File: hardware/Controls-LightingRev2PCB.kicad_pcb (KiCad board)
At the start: 2 copper layers, 50 x 53.5 mm, 53 parts, among them IC1 LM74502HDDFR, IC3 TLV70130DBVR, J1 MX150_02x08_RightAngle, J3 53307-2471, Q2 IRLML0030, Q3 IRLML0030, Q4 PSMN8R5-40MSDX, U1 TLV2371DBV, U2 INA241A5xD, U3 INA241A5xD, U4 INA241A5xD, U5 SN74LV1T34DBV, U8 TLV2371DBV, U9 TLV2371DBV

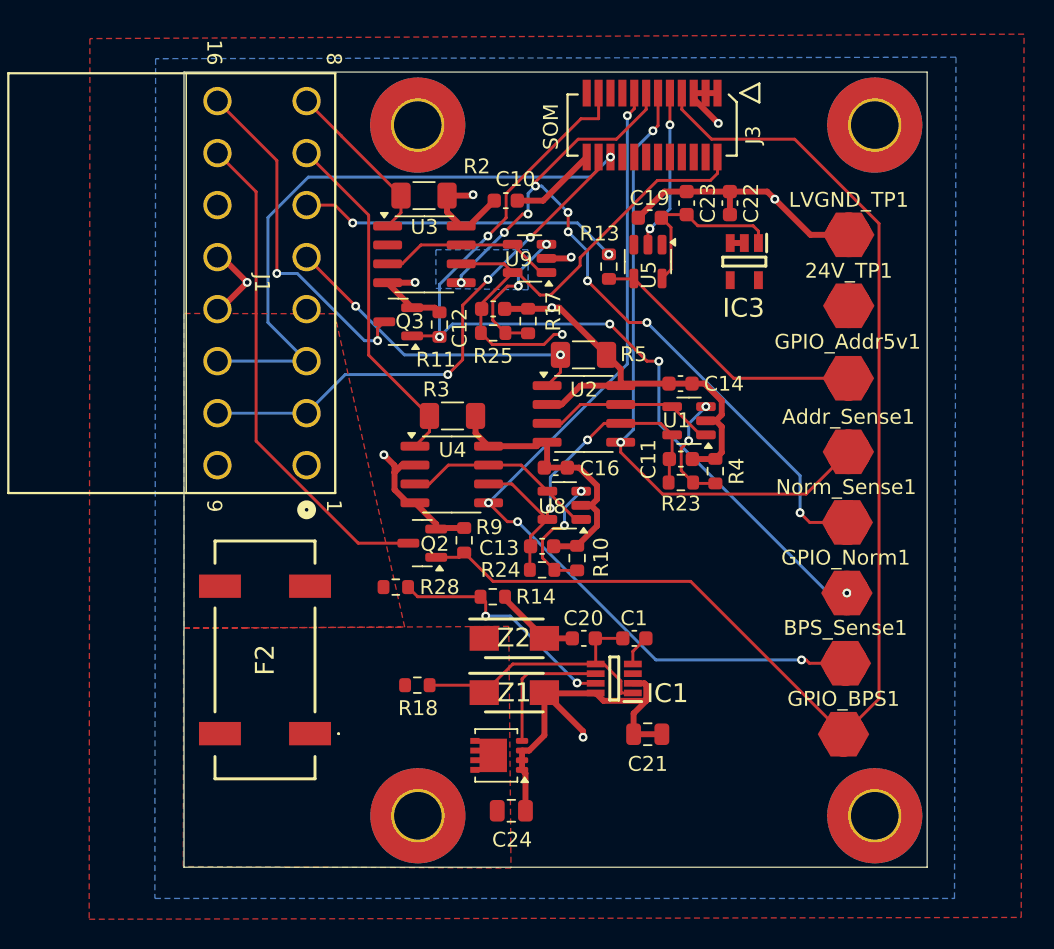
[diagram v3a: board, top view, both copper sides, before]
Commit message: Test points added
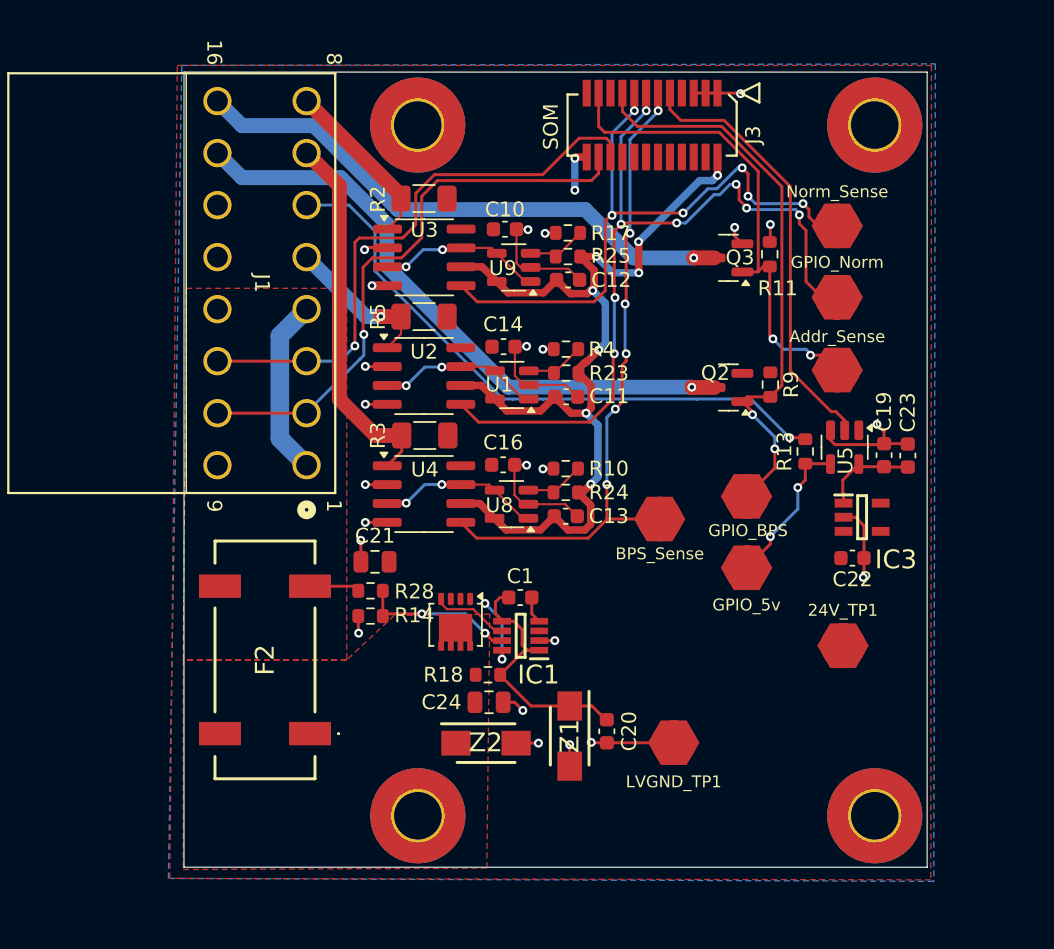
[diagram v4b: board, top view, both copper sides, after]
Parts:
- removed Addr_Sense1, BPS_Sense1, GPIO_Addr5v1, GPIO_BPS1, GPIO_Norm1, Norm_Sense1: TestPoint, UTSVT_Special:TestPoint_HEX_3mmID
- added Addr_Sense: TestPoint, UTSVT_Special:TestPoint_HEX_3mmID, F.Cu at (124.8, 37.0)
- added BPS_Sense: TestPoint, UTSVT_Special:TestPoint_HEX_3mmID, F.Cu at (112.8, 51.9)
- added GPIO_5v: TestPoint, UTSVT_Special:TestPoint_HEX_3mmID, F.Cu at (118.7, 55.2)
- added GPIO_BPS: TestPoint, UTSVT_Special:TestPoint_HEX_3mmID, F.Cu at (118.7, 50.4)
- added GPIO_Norm: TestPoint, UTSVT_Special:TestPoint_HEX_3mmID, F.Cu at (124.8, 41.9)
- added Norm_Sense: TestPoint, UTSVT_Special:TestPoint_HEX_3mmID, F.Cu at (124.8, 32.2)
- moved LVGND_TP1 36.1 mm to (113.8, 67.0)
- moved C22 25.3 mm to (125.8, 54.5), turned to 180 degrees
- moved Q2 23.1 mm to (117.5, 43.1)
- moved R9 23.1 mm to (120.3, 42.9)
- moved 24V_TP1 22.9 mm to (125.2, 60.4)
- moved R11 22.7 mm to (120.3, 34.1)
- moved Q3 22.6 mm to (117.5, 34.4)
- moved C23 22.6 mm to (129.6, 47.6)
- moved C19 22.4 mm to (128.0, 47.6), turned to -90 degrees
- moved C21 21.7 mm to (93.7, 54.8)
- moved IC3 18.9 mm to (126.5, 51.8), turned to 0 degrees
- moved U5 18.2 mm to (125.3, 47.1)
- moved R13 18.1 mm to (122.7, 47.4)
- moved R4 13.0 mm to (106.5, 40.5), turned to 180 degrees
- moved C14 12.2 mm to (102.3, 40.3)
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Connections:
- C10 pad 1: +24V -> Addressable_GND
- C11 pad 1: +24V -> Addressable_GND
- C12 pad 1: +24V -> Addressable_GND
- C13 pad 1: +24V -> Addressable_GND
- C14 pad 1: +24V -> Addressable_GND
- C16 pad 1: +24V -> Addressable_GND
- C19 pad 1: +24V -> Addressable_GND
- C20 pad 1: +24V -> Addressable_GND
- C21 pad 2: +24V -> Addressable_GND
- C22 pad 1: +24V -> Addressable_GND
- C23 pad 1: +24V -> Addressable_GND
- C24 pad 2: +24V -> Addressable_GND
- IC1 pad 2: +24V -> Addressable_GND
- IC3 pad 2: +24V -> Addressable_GND
- J1 pad 12: +24V -> Addressable_GND
- J1 pad 13: +24V -> Addressable_GND
- J3 pad 1: +24V -> Addressable_GND
- J3 pad 11: ADDR_Sense -> BPS_Sense
- J3 pad 13: NORMAL_Sense -> ADDR_Sense
- J3 pad 15: BPS_Sense -> NORMAL_Sense
- J3 pad 17: unconnected-(J3-SPI1_MOSI-Pad17) -> GPIO_BPS_Strobe
- J3 pad 3: +24V -> Addressable_GND
- J3 pad 5: +24V -> Addressable_GND
- J3 pad 7: GPIO_BPS_Strobe -> unconnected-(J3-OPAMP1_VINP-Pad7)
- LVGND_TP1 pad 1: +24V -> Addressable_GND
- Q2 pad 2: +24V -> Addressable_GND
- Q3 pad 2: +24V -> Addressable_GND
- R10 pad 2: +24V -> Addressable_GND
- R11 pad 1: +24V -> Addressable_GND
- R14 pad 2: +24V -> Addressable_GND
- R17 pad 2: +24V -> Addressable_GND
- R4 pad 2: +24V -> Addressable_GND
- R9 pad 1: +24V -> Addressable_GND
- U1 pad 2: +24V -> Addressable_GND
- U2 pad 2: +24V -> Addressable_GND
- U2 pad 4: +24V -> Addressable_GND
- U3 pad 4: +24V -> Addressable_GND
- U4 pad 2: +24V -> Addressable_GND
- U4 pad 4: +24V -> Addressable_GND
- U8 pad 2: +24V -> Addressable_GND
- U9 pad 2: +24V -> Addressable_GND
- Z1 pad 2: +24V -> Addressable_GND
- Z2 pad 2: +24V -> Addressable_GND
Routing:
- net +24V: track 141.5 -> 7.81 mm, vias 9 -> 4
- net Addressable_GND: track 0.00 -> 65.8 mm, vias 0 -> 24
- net GPIO_BPS_Strobe: track 85.5 -> 38.6 mm, vias 0 -> 2
- net GPIO_Normal: track 61.1 -> 33.6 mm, vias 5 -> 2
- net Addressable_Logic: track 21.7 -> 41.6 mm, vias 2 -> 1
- net GPIO_Addr: track 10.8 -> 29.5 mm, vias 2 -> 0
- net BPS_Sense: track 60.1 -> 44.5 mm, vias 4 -> 6
- net 24V_Ext: track 0.00 -> 15.4 mm
- net Normal_GND: track 23.4 -> 37.8 mm, vias 2 -> 1
- net ADDR_Sense: track 42.9 -> 55.7 mm, vias 2 -> 8
- net Addressable_PWR: track 22.2 -> 10.5 mm, vias 2 -> 1
- net +3.3V: track 59.0 -> 68.0 mm, vias 3 -> 8
- net GPIO_Addr5V: track 18.9 -> 10.4 mm, vias 0 -> 2
- net Strobe_GND: track 33.5 -> 41.6 mm, vias 0 -> 1
- net NORMAL_Sense: track 53.4 -> 45.9 mm, vias 9 -> 6
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- added copper zone on F.Cu, net +24V
- added copper zone on B.Cu, net Addressable_GND
- removed copper zone on B.Cu, net +24V
- removed copper zone on B.Cu, net +3.3V
- removed copper zone on F.Cu, net Addressable_GND

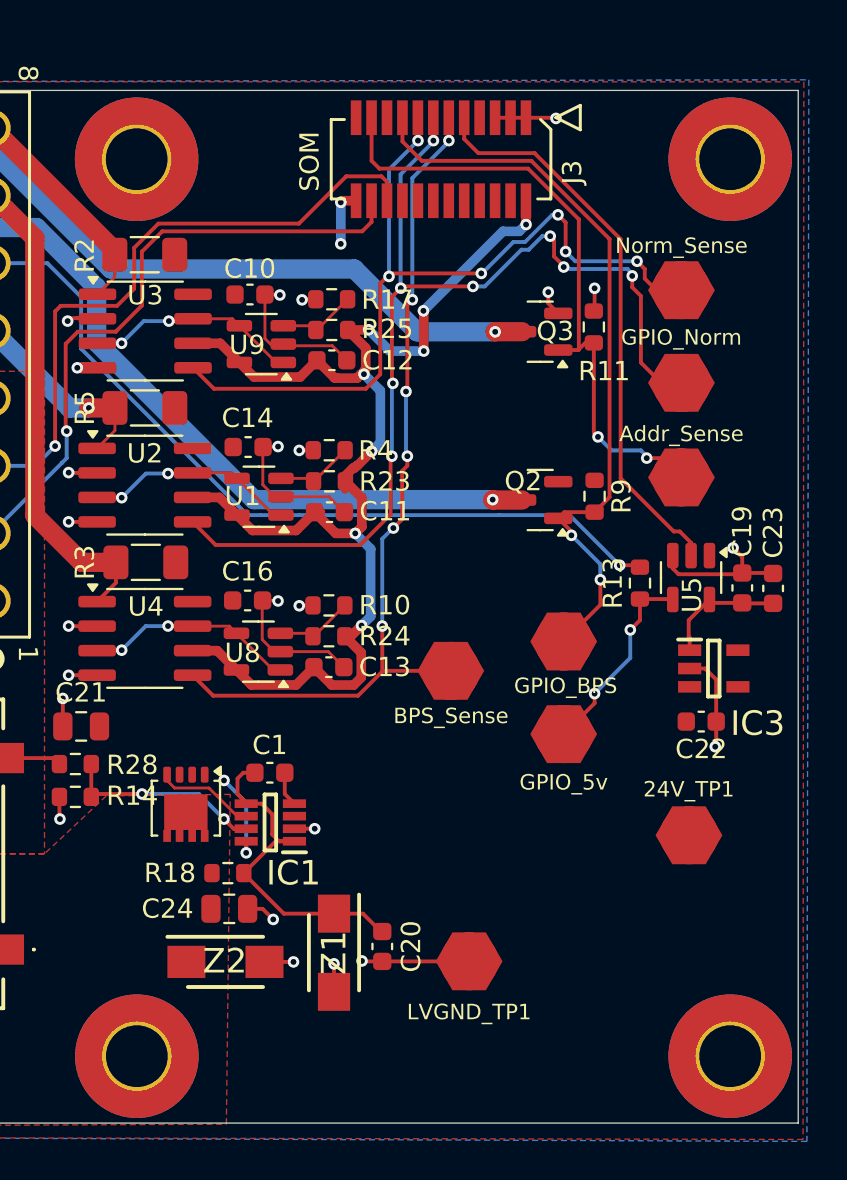
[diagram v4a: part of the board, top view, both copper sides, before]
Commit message: slight test point and keep out updates
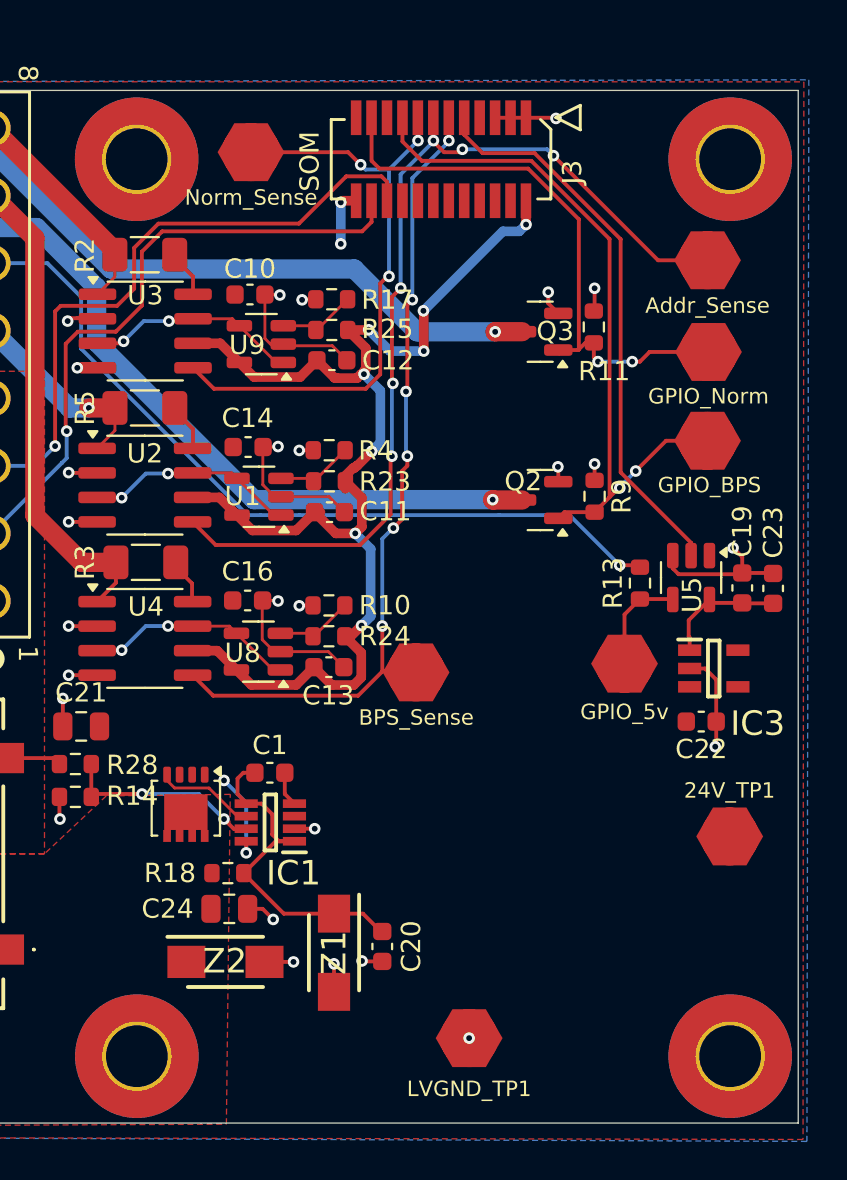
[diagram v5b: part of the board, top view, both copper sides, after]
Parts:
- moved Norm_Sense 23.4 mm to (102.5, 25.1)
- moved GPIO_BPS 12.8 mm to (126.2, 40.0)
- moved GPIO_Norm 6.65 mm to (126.2, 35.4)
- moved Addr_Sense 6.49 mm to (126.2, 30.6)
- moved GPIO_5v 4.82 mm to (121.8, 51.5)
- moved LVGND_TP1 3.98 mm to (113.8, 71.0)
- moved 24V_TP1 2.11 mm to (127.3, 60.5)
- moved BPS_Sense 1.80 mm to (111.0, 52.0)
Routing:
- net NORMAL_Sense: track 45.9 -> 32.1 mm, vias 6 -> 3
- net +24V: track 7.81 -> 14.8 mm
- net ADDR_Sense: track 55.7 -> 50.0 mm, vias 8 -> 6
- net GPIO_Addr5V: track 10.4 -> 5.39 mm, vias 2 -> 0
- net GPIO_Normal: track 33.6 -> 30.2 mm
- net Addressable_GND: track 65.8 -> 62.9 mm, vias 24 -> 27
- net BPS_Sense: track 44.5 -> 42.8 mm
- net GPIO_BPS_Strobe: track 38.6 -> 36.9 mm

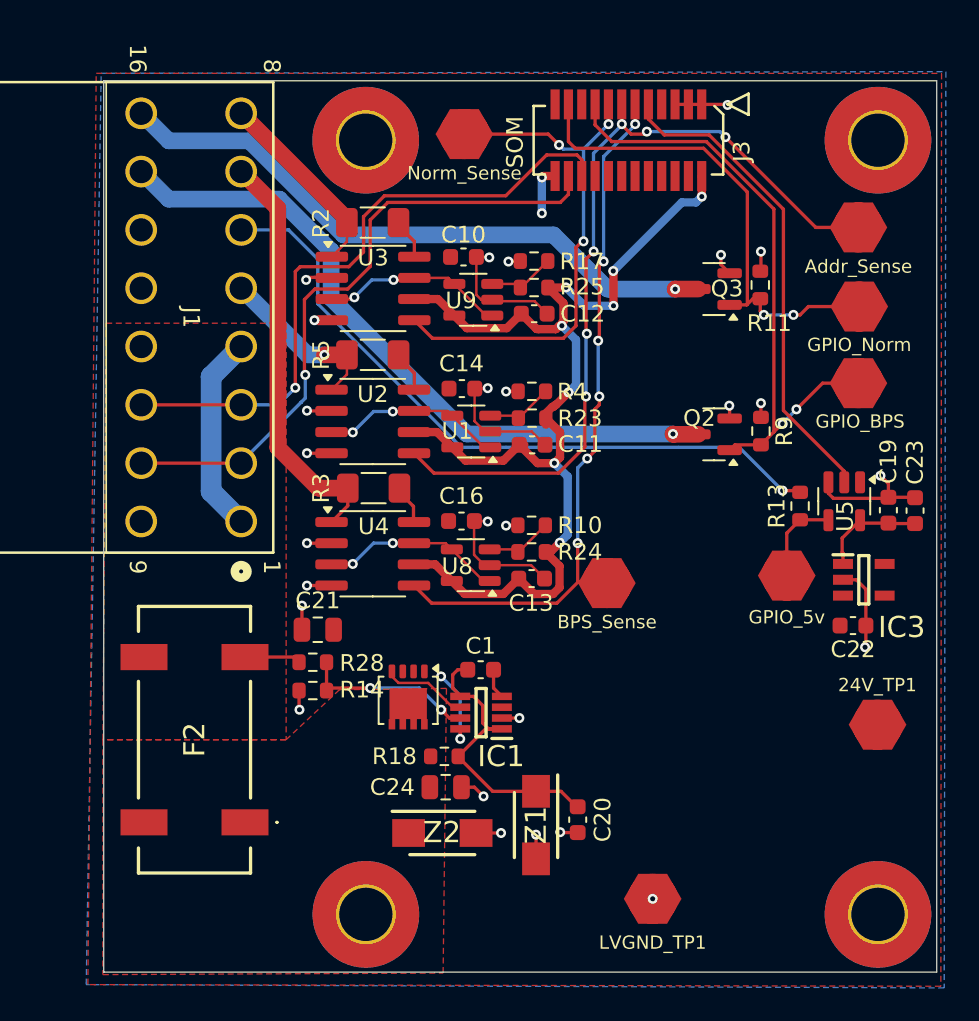
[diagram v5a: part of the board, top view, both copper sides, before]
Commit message: rounded corners + gerbers
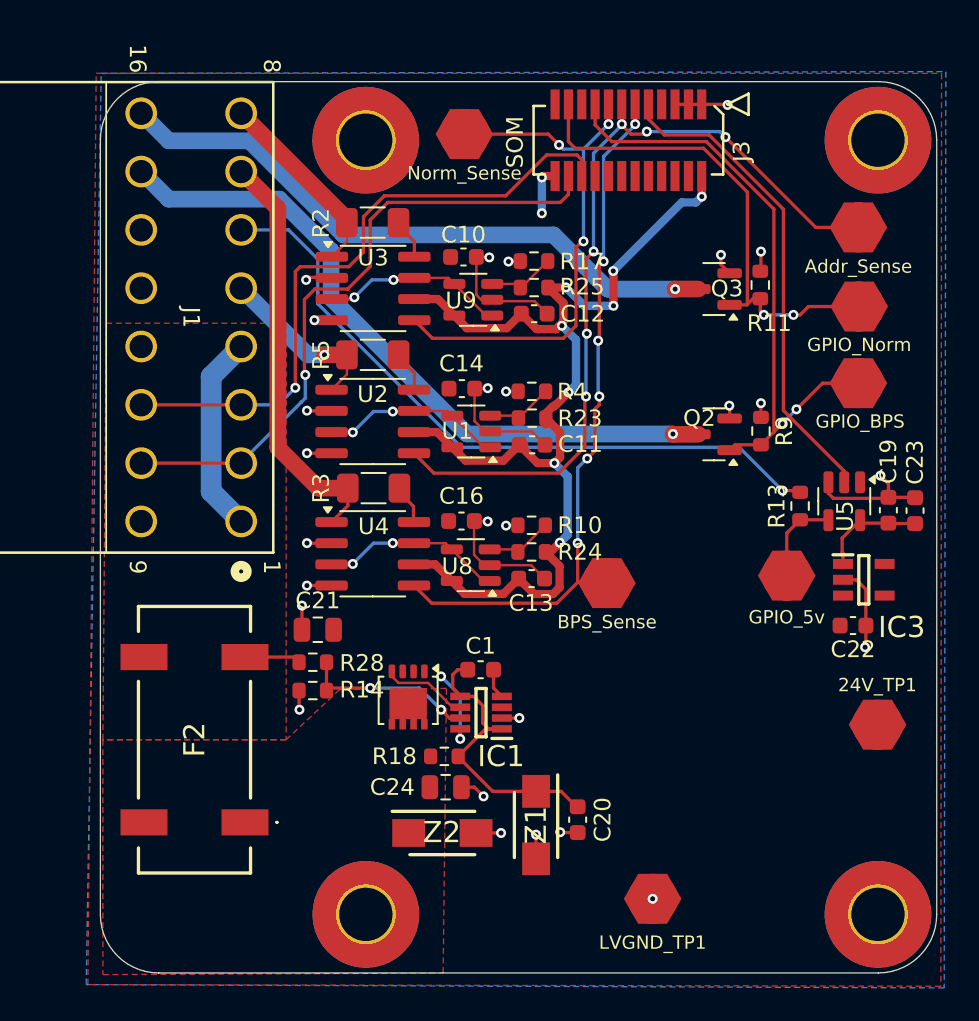
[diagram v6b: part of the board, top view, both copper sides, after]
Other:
- board size 50 x 53.5 mm -> 50.2 x 53.5 mm
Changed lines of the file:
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@@
 		)
 	)
-	(gr_rect
-		(start 80.85 21.85)
-		(end 130.85 75.35)
+	(gr_line
+		(start 127.35 21.9)
+		(end 84.15 21.9)
 		(stroke
 			(width 0.05)
-			(type solid)
+			(type default)
 		)
-		(fill no)
 		(layer "Edge.Cuts")
 	)
+	(gr_arc
+		(start 84.15 75.4)
+		(mid 81.675126 74.374874)
+		(end 80.65 71.9)
+		(stroke
+			(width 0.05)
+			(type default)
+		)
+		(layer "Edge.Cuts")
+	)
+	(gr_line
+		(start 130.85 71.9)
+		(end 130.85 25.4)
+		(stroke
+			(width 0.05)
+			(type default)
+		)
+		(layer "Edge.Cuts")
+	)
+	(gr_line
+		(start 84.15 75.4)
+		(end 127.35 75.4)
+		(stroke
+			(width 0.05)
+			(type default)
+		)
+		(layer "Edge.Cuts")
+	)
+	(gr_line
+		(start 80.65 25.4)
+		(end 80.65 71.9)
+		(stroke
+			(width 0.05)
+			(type default)
+		)
+		(layer "Edge.Cuts")
+	)
+	(gr_arc
+		(start 80.65 25.4)
+		(mid 81.675126 22.925126)
+		(end 84.15 21.9)
+		(stroke
+			(width 0.05)
+			(type default)
+		)
+		(layer "Edge.Cuts")
+	)
+	(gr_arc
+		(start 130.85 71.9)
+		(mid 129.824874 74.374874)
+		(end 127.35 75.4)
+		(stroke
+			(width 0.05)
+			(type default)
+		)
+		(layer "Edge.Cuts")
+	)
+	(gr_arc
+		(start 127.35 21.9)
+		(mid 129.824874 22.925126)
+		(end 130.85 25.4)
+		(stroke
+			(width 0.05)
+			(type default)
+		)
+		(layer "Edge.Cuts")
+	)
